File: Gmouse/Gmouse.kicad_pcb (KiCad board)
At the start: 2 copper layers, 80 x 100 mm, 79 parts, among them J1 Motor_RF, J2 Motor_RR, J3 Motor_LF, J4 Motor_LR, J5 Conn_01x08_Pin, Q10 SFH300, Q12 SFH300, Q14 BC847, Q2 SFH300, Q4 SFH300, Q6 SFH300, Q8 SFH300, U1 Teensy4.0, U2 TB6612FNG, U3 L78L05_SOT89, U4 HCMS-2903, U5 TB6612FNG, U7 LD1117S33TR_SOT223

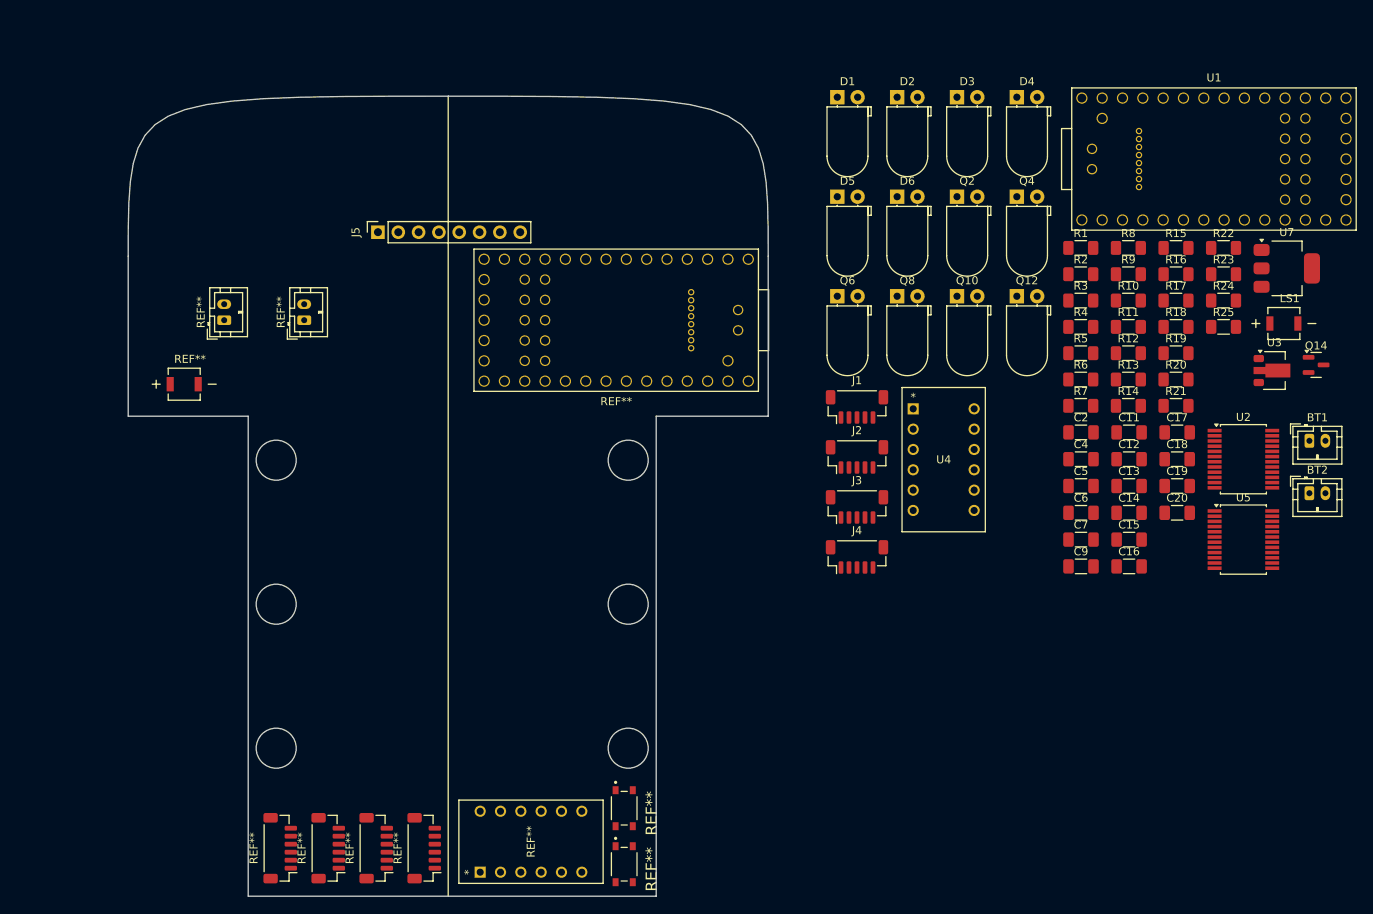
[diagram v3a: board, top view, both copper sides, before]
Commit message: starts pcb design and assigns ton of pins
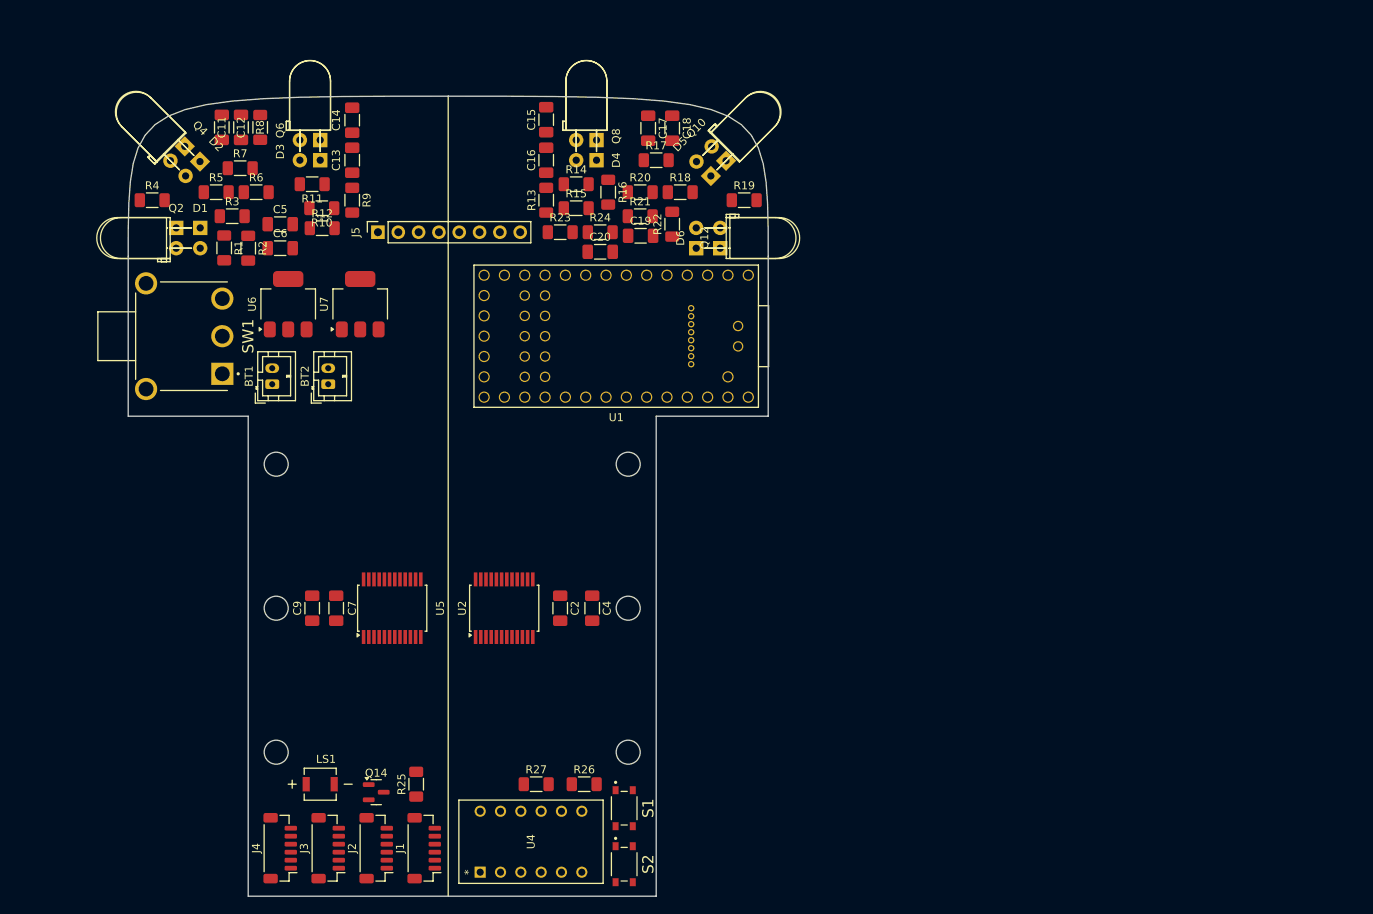
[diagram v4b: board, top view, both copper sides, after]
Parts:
- removed REF** (x2): JST_PH_B2B-PH-K_1x02_P2.00mm_Vertical, Connector_JST:JST_PH_B2B-PH-K_1x02_P2.00mm_Vertical
- removed REF** (x4): JST_SH_BM06B-SRSS-TB_1x06-1MP_P1.00mm_Vertical, Connector_JST:JST_SH_BM06B-SRSS-TB_1x06-1MP_P1.00mm_Vertical
- removed REF**: DIP12_HCMS-290X-A_BRA, HCMS_2903:DIP12_HCMS-290X-A_BRA
- removed REF**: Teensy 4.0, Teensy:Teensy40_SMT
- removed REF** (x2): SW_TL3365AF180QG, Buttons:SW_TL3365AF180QG
- removed REF**: XDCR_SMT-0440-T-R, SMT_0440:XDCR_SMT-0440-T-R
- removed U3: L78L05_SOT89, Package_TO_SOT_SMD:SOT-89-3
- added R26: 10K, Resistor_SMD:R_1206_3216Metric_Pad1.30x1.75mm_HandSolder, F.Cu at (111.0, 126.0)
- added R27: 10K, Resistor_SMD:R_1206_3216Metric_Pad1.30x1.75mm_HandSolder, F.Cu at (105.0, 126.0)
- added S1: TL3365AF180QG, Buttons:SW_TL3365AF180QG, F.Cu at (116.0, 129.0)
- added S2: TL3365AF180QG, Buttons:SW_TL3365AF180QG, F.Cu at (116.0, 136.0)
- added SW1: SW_SPDT, Switch:SW_500SSP1S1M6QEA, F.Cu at (61.0, 70.0)
- added U6: LD1117S50TR_SOT223, Package_TO_SOT_SMD:SOT-223-3_TabPin2, F.Cu at (74.0, 66.0)
- D1, D2, D3, D4, D5, D6: footprint LED_THT:LED_D5.0mm_Horizontal_O1.27mm_Z9.0mm -> LED_THT:LED_D5.0mm_Horizontal_O3.81mm_Z9.0mm
- J1, J2, J3, J4: footprint Connector_JST:JST_SH_BM05B-SRSS-TB_1x05-1MP_P1.00mm_Vertical -> Connector_JST:JST_SH_BM06B-SRSS-TB_1x06-1MP_P1.00mm_Vertical
- moved LS1 133.5 mm to (78.0, 126.0)
- moved BT1 129.8 mm to (72.0, 76.0), turned to 90 degrees
- moved Q14 129.1 mm to (85.0, 127.0)
- moved BT2 123.4 mm to (79.0, 76.0), turned to 90 degrees
- moved C11 119.6 mm to (65.7, 43.9), turned to -90 degrees
- moved C12 118.5 mm to (68.1, 43.9), turned to -90 degrees
- moved R4 117.1 mm to (57.0, 53.0)
- moved R25 116.0 mm to (90.0, 126.0), turned to 90 degrees
- moved U7 115.9 mm to (83.0, 66.0), turned to 90 degrees
- moved R5 109.9 mm to (65.0, 52.0)
- moved R8 109.6 mm to (70.5, 43.9), turned to 90 degrees
- moved R7 109.2 mm to (68.0, 49.0)
- moved C14 108.8 mm to (82.0, 43.0), turned to 90 degrees
- moved R1 107.1 mm to (66.0, 59.0), turned to -90 degrees
- moved U5 106.7 mm to (87.0, 104.0), turned to 90 degrees
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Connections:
- J5 pad 1: unconnected-(J5-Pin_1-Pad1) -> +5V
- J5 pad 3: unconnected-(J5-Pin_3-Pad3) -> GND
- J5 pad 4: unconnected-(J5-Pin_4-Pad4) -> Gyro_SCL
- J5 pad 5: unconnected-(J5-Pin_5-Pad5) -> Gyro_SDA
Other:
- outline, holes or cut-outs redrawn
- copper layers 2 -> 4

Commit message: cleaned up IR Emitter Circuit
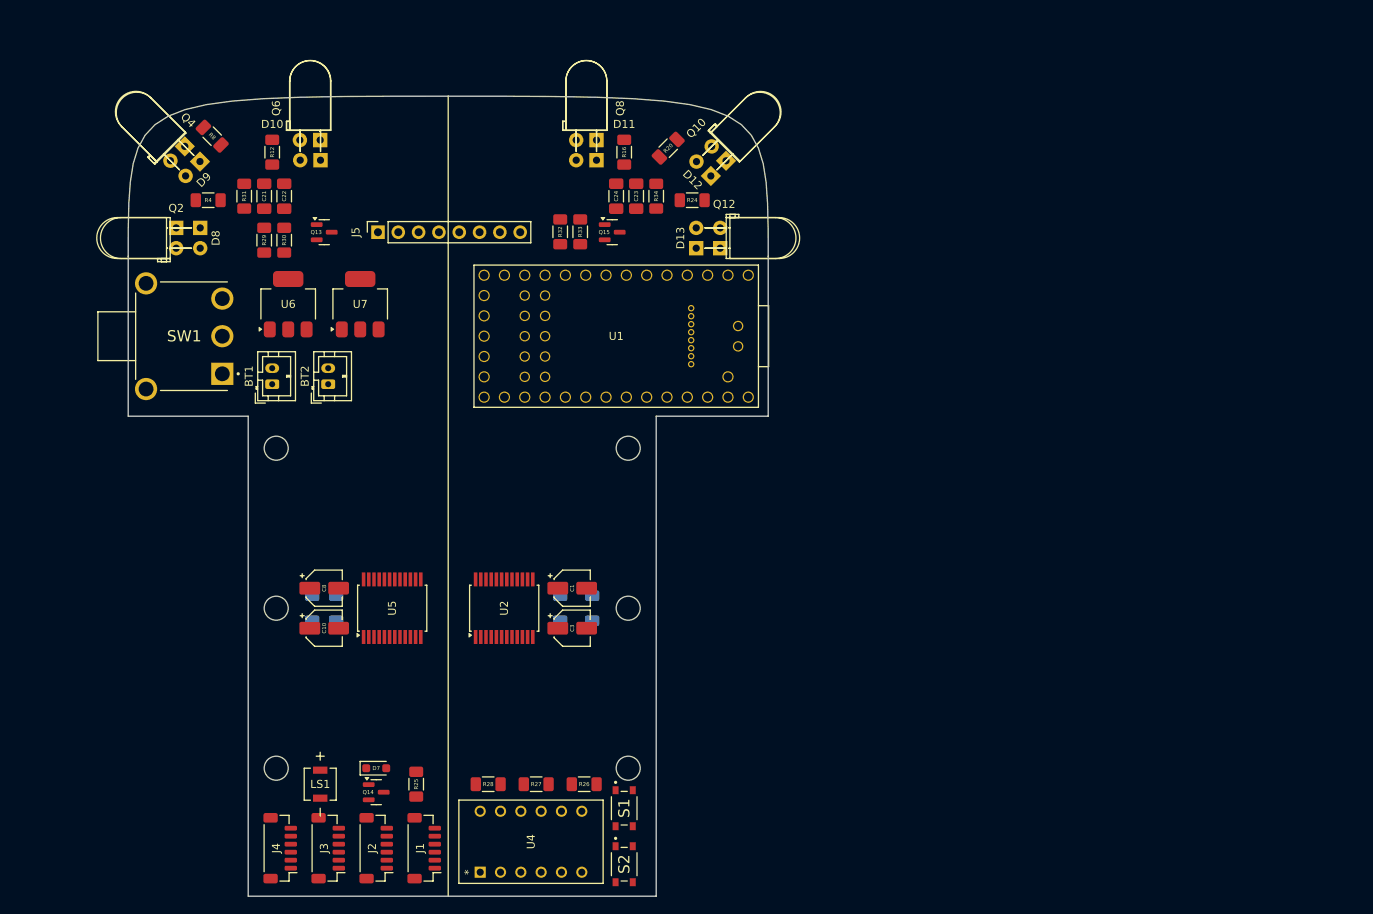
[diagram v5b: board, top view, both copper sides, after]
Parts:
- removed C11, C13, C15, C17, C19, C5: 4.7uF, Capacitor_SMD:C_1206_3216Metric_Pad1.33x1.80mm_HandSolder
- removed C12, C14, C16, C18, C20, C6: 0.1uF, Capacitor_SMD:C_1206_3216Metric_Pad1.33x1.80mm_HandSolder
- removed D1, D2, D3, D4, D5, D6: IR, LED_THT:LED_D5.0mm_Horizontal_O3.81mm_Z9.0mm
- removed R1, R10, R14, R18, R22, R6: 47K, Resistor_SMD:R_1206_3216Metric_Pad1.30x1.75mm_HandSolder
- removed R11, R15, R19, R23, R3, R7: 51, Resistor_SMD:R_1206_3216Metric_Pad1.30x1.75mm_HandSolder
- removed R13, R17, R2, R21, R5, R9: 100, Resistor_SMD:R_1206_3216Metric_Pad1.30x1.75mm_HandSolder
- added C1: 10 uF, Capacitor_SMD:CP_Elec_4x5.4, F.Cu at (109.5, 101.5)
- added C10: 10 uF, Capacitor_SMD:CP_Elec_4x5.4, F.Cu at (78.5, 106.5)
- added C21: 4.7uF, Capacitor_SMD:C_1206_3216Metric_Pad1.33x1.80mm_HandSolder, F.Cu at (71.0, 52.5)
- added C22: 0.1uF, Capacitor_SMD:C_1206_3216Metric_Pad1.33x1.80mm_HandSolder, F.Cu at (73.5, 52.5)
- added C23: 4.7uF, Capacitor_SMD:C_1206_3216Metric_Pad1.33x1.80mm_HandSolder, F.Cu at (117.5, 52.5)
- added C24: 0.1uF, Capacitor_SMD:C_1206_3216Metric_Pad1.33x1.80mm_HandSolder, F.Cu at (115.0, 52.5)
- added C3: 10 uF, Capacitor_SMD:CP_Elec_4x5.4, F.Cu at (109.5, 106.5)
- added C8: 10 uF, Capacitor_SMD:CP_Elec_4x5.4, F.Cu at (78.5, 101.5)
- added D10: IR, LED_THT:LED_D5.0mm_Horizontal_O3.81mm_Z9.0mm, F.Cu at (78.0, 48.0)
- added D11: IR, LED_THT:LED_D5.0mm_Horizontal_O3.81mm_Z9.0mm, F.Cu at (112.5, 48.0)
- added D12: IR, LED_THT:LED_D5.0mm_Horizontal_O3.81mm_Z9.0mm, F.Cu at (126.8, 50.0)
- added D13: IR, LED_THT:LED_D5.0mm_Horizontal_O3.81mm_Z9.0mm, F.Cu at (125.0, 59.0)
- added D7: D, Diode_SMD:D_SOD-323_HandSoldering, F.Cu at (85.0, 124.0)
- added D8: IR, LED_THT:LED_D5.0mm_Horizontal_O3.81mm_Z9.0mm, F.Cu at (63.0, 56.5)
- added D9: IR, LED_THT:LED_D5.0mm_Horizontal_O3.81mm_Z9.0mm, F.Cu at (63.0, 48.2)
- added Q13: NMOS, Package_TO_SOT_SMD:SOT-23, F.Cu at (78.5, 57.0)
- added Q15: NMOS, Package_TO_SOT_SMD:SOT-23, F.Cu at (114.5, 57.0)
- added R28: 10K, Resistor_SMD:R_1206_3216Metric_Pad1.30x1.75mm_HandSolder, F.Cu at (99.0, 126.0)
- added R29: 100, Resistor_SMD:R_1206_3216Metric_Pad1.30x1.75mm_HandSolder, F.Cu at (71.0, 58.0)
- added R30: 47K, Resistor_SMD:R_1206_3216Metric_Pad1.30x1.75mm_HandSolder, F.Cu at (73.5, 58.0)
- added R31: 51, Resistor_SMD:R_1206_3216Metric_Pad1.30x1.75mm_HandSolder, F.Cu at (68.5, 52.5)
- added R32: 100, Resistor_SMD:R_1206_3216Metric_Pad1.30x1.75mm_HandSolder, F.Cu at (108.0, 57.0)
- added R33: 47K, Resistor_SMD:R_1206_3216Metric_Pad1.30x1.75mm_HandSolder, F.Cu at (110.5, 57.0)
- added R34: 51, Resistor_SMD:R_1206_3216Metric_Pad1.30x1.75mm_HandSolder, F.Cu at (120.0, 52.5)
- C2, C4, C7, C9: moved to B.Cu
- moved R24 12.2 mm to (124.5, 53.0), turned to 180 degrees
- moved R12 11.4 mm to (72.0, 47.0), turned to -90 degrees
- moved R4 7.00 mm to (64.0, 53.0)
- moved R20 6.52 mm to (121.5, 46.5), turned to -135 degrees
- moved R8 6.10 mm to (64.5, 45.0), turned to -45 degrees
- moved R16 5.39 mm to (116.0, 47.0)
- turned LS1 to -90 degrees
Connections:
- net Motor1_M1 renamed Motor_RF_M1
- net Motor1_M2 renamed Motor_RF_M2
- net Motor2_M1 renamed Motor_RR_M1
- net Motor2_M2 renamed Motor_RR_M2
- J1 pad 2: Motor1_OutB -> Motor_RF_OutB
- J1 pad 3: Motor1_OutA -> Motor_RF_OutA
- J2 pad 2: Motor2_OutB -> Motor_RR_OutB
- J2 pad 3: Motor2_OutA -> Motor_RR_OutA
- U1 pad 10: unconnected-(U1-8_TX2_IN1-Pad10) -> Motor_STBY
- U1 pad 11: unconnected-(U1-9_OUT1C-Pad11) -> Speaker Signal
- U1 pad 12: unconnected-(U1-10_CS_MQSR-Pad12) -> HCMS_CE
- U1 pad 13: unconnected-(U1-11_MOSI_CTX1-Pad13) -> HCMS_DataIn
- U1 pad 14: unconnected-(U1-12_MISO_MQSL-Pad14) -> HCMS_RS
- U1 pad 20: unconnected-(U1-13_SCK_CRX1_LED-Pad20) -> HCMS_CLK
- U1 pad 21: unconnected-(U1-14_A0_TX3_SPDIF_OUT-Pad21) -> Motor_RF_OutA
- U1 pad 22: unconnected-(U1-15_A1_RX3_SPDIF_IN-Pad22) -> Motor_RF_OutB
- U1 pad 23: unconnected-(U1-16_A2_RX4_SCL1-Pad23) -> Gyro_SCL
- U1 pad 24: unconnected-(U1-17_A3_TX4_SDA1-Pad24) -> Gyro_SDA
- U1 pad 25: unconnected-(U1-18_A4_SDA0-Pad25) -> IR_Reciever_Left_90
- U1 pad 26: unconnected-(U1-19_A5_SCL0-Pad26) -> IR_Reciever_Left_45
- U1 pad 27: unconnected-(U1-20_A6_TX5_LRCLK1-Pad27) -> IR_Reciever_Left_0
- U1 pad 28: unconnected-(U1-21_A7_RX5_BCLK1-Pad28) -> IR_Reciever_Right_0
- U1 pad 29: unconnected-(U1-22_A8_CTX1-Pad29) -> IR_Reciever_Right_45
- U1 pad 30: unconnected-(U1-23_A9_CRX1_MCLK1-Pad30) -> IR_Reciever_Right_90
- U1 pad 35: unconnected-(U1-24_A10_TX6_SCL2-Pad35) -> Left_IN1
- U1 pad 36: unconnected-(U1-25_A11_RX6_SDA2-Pad36) -> Right_IN1
- U1 pad 37: unconnected-(U1-26_A12_MOSI1-Pad37) -> Left_IN2
- U1 pad 38: unconnected-(U1-27_A13_SCK1-Pad38) -> Right_IN2
- U1 pad 39: unconnected-(U1-28_RX7-Pad39) -> Motor_RR_OutA
- U1 pad 40: unconnected-(U1-29_TX7-Pad40) -> Motor_RR_OutB
- U1 pad 41: unconnected-(U1-30_CRX3-Pad41) -> Motor_LF_OutA
- U1 pad 42: unconnected-(U1-31_CTX3-Pad42) -> Motor_LF_OutB
- U1 pad 43: unconnected-(U1-32_OUT1B-Pad43) -> Motor_LR_OutA
- U1 pad 44: unconnected-(U1-33_MCLK2-Pad44) -> Motor_LR_OutB
- U1 pad 45: unconnected-(U1-34_DAT1_MISO2-Pad45) -> Interface_Button1
- U1 pad 46: unconnected-(U1-35_DAT0_MOSI2-Pad46) -> Interface_Button2
- U1 pad 6: unconnected-(U1-4_BCLK2-Pad6) -> Motor_RF_PWM
- U1 pad 7: unconnected-(U1-5_IN2-Pad7) -> Motor_RR_PWM
- U1 pad 8: unconnected-(U1-6_OUT1D-Pad8) -> Motor_LF_PWM
- U1 pad 9: unconnected-(U1-7_RX2_OUT1A-Pad9) -> Motor_LR_PWM
- U2 pad 15: Motor2_PWM -> Motor_RR_PWM
- U2 pad 23: Motor1_PWM -> Motor_RF_PWM
- U4 pad 10: +5V -> +3V3
- U4 pad 11: +5V -> +3V3
- U4 pad 12: HCMS_Reset -> Net-(U4-*RESET)
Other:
- outline, holes or cut-outs redrawn

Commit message: Started adding traces
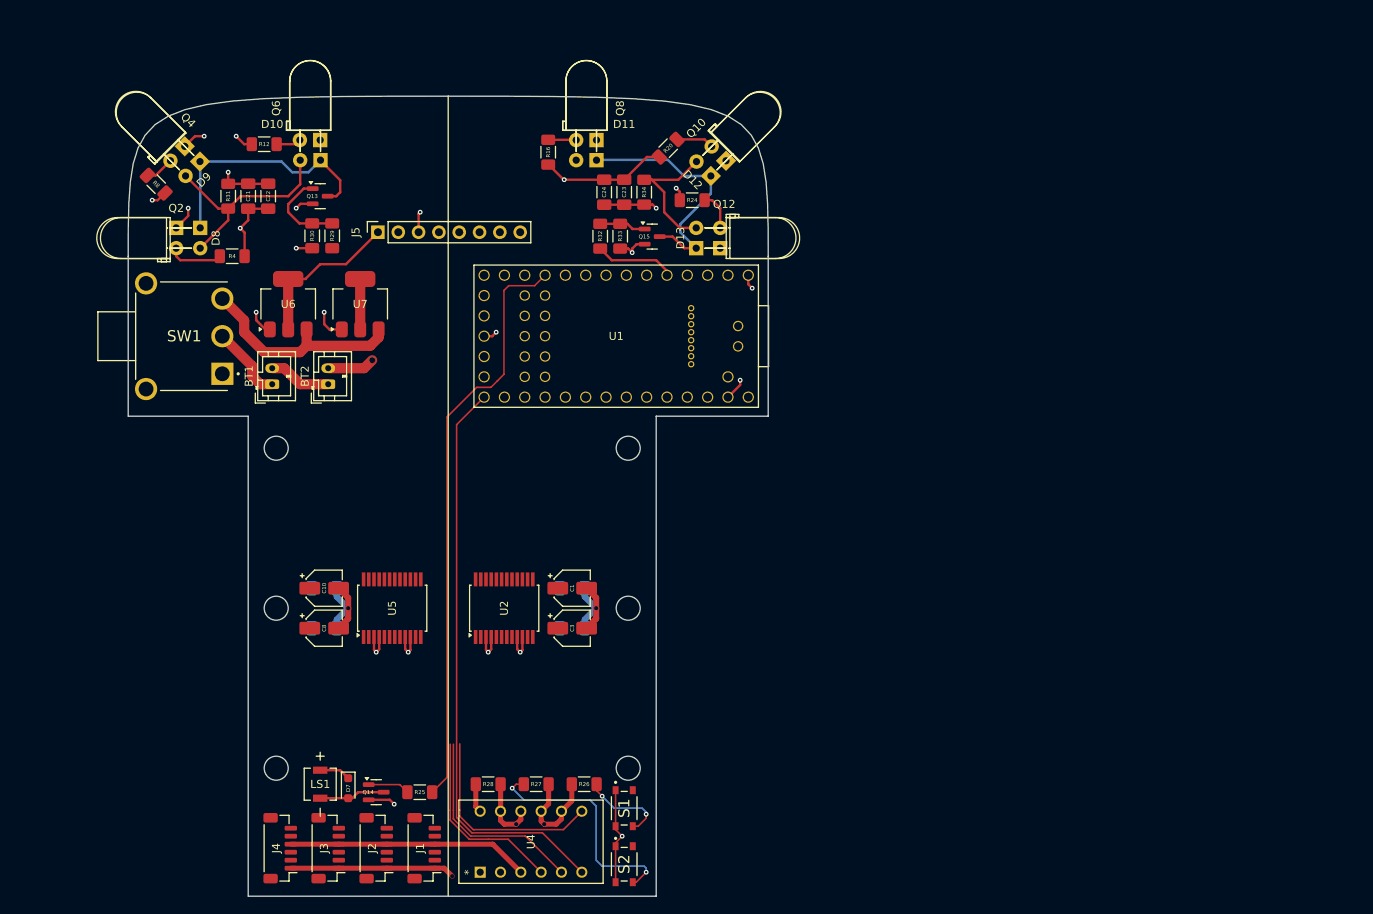
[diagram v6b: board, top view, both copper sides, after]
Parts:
- moved R16 9.50 mm to (106.5, 47.0)
- moved R8 9.22 mm to (57.5, 51.0)
- moved R29 8.52 mm to (79.5, 57.5)
- moved R4 7.62 mm to (67.0, 60.0)
- moved Q15 5.03 mm to (119.5, 57.5)
- moved R32 5.03 mm to (113.0, 57.5)
- moved R33 5.03 mm to (115.5, 57.5)
- moved C10 5.00 mm to (78.5, 101.5)
- moved C8 5.00 mm to (78.5, 106.5)
- moved Q13 4.53 mm to (78.0, 52.5)
- moved D7 4.30 mm to (81.5, 126.5), turned to -90 degrees
- moved R30 3.54 mm to (77.0, 57.5)
- moved C4 3.54 mm to (109.5, 106.5), turned to 0 degrees
- moved C2 2.92 mm to (109.5, 101.5), turned to 0 degrees
- moved C7 2.92 mm to (78.5, 106.5), turned to 0 degrees
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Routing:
- net GND: track 0.00 -> 138.7 mm, vias 0 -> 24
- net Speaker Signal: track 0.00 -> 73.4 mm
- net HCMS_CLK: track 0.00 -> 72.4 mm
- net +5V: track 0.00 -> 50.1 mm
- net +3V3: track 0.00 -> 50.1 mm, vias 0 -> 6
- net Net-(D11-K): track 0.00 -> 31.8 mm
- net Net-(D10-K): track 0.00 -> 31.3 mm
- net Net-(R27-Pad1): track 0.00 -> 29.2 mm, vias 0 -> 2
- net +BATT: track 0.00 -> 27.0 mm
- net Net-(D10-A): track 0.00 -> 26.7 mm
- net HCMS_CE: track 0.00 -> 25.9 mm
- net HCMS_RS: track 0.00 -> 25.6 mm
- net HCMS_DataIn: track 0.00 -> 23.6 mm
- net Net-(D11-A): track 0.00 -> 17.9 mm
- net Net-(R26-Pad2): track 0.00 -> 11.0 mm, vias 0 -> 2
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
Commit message: Lot of Manual Routing
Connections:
- C3 pad 1: +5V -> +3V3
- C4 pad 1: +5V -> +3V3
- C7 pad 1: +5V -> +3V3
- C8 pad 1: +5V -> +3V3
- J1 pad 4: +5V -> +3V3
- J2 pad 4: +5V -> +3V3
- J3 pad 4: +5V -> +3V3
- J4 pad 4: +5V -> +3V3
- J5 pad 1: +5V -> +3V3
- U1 pad 39: Motor_RR_OutA -> Motor_RR_OutB
- U1 pad 40: Motor_RR_OutB -> Motor_RR_OutA
- U1 pad 41: Motor_LF_OutA -> Motor_LF_OutB
- U1 pad 42: Motor_LF_OutB -> Motor_LF_OutA
- U1 pad 43: Motor_LR_OutA -> Motor_LR_OutB
- U1 pad 44: Motor_LR_OutB -> Motor_LR_OutA
- U2 pad 20: +5V -> +3V3
- U5 pad 20: +5V -> +3V3
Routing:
- net +5V: track 50.1 -> 197.7 mm, vias 0 -> 1
- net +BATT: track 27.0 -> 152.9 mm, vias 0 -> 4
- net Motor_LR_OutB: track 0.00 -> 104.1 mm, vias 0 -> 1
- net Motor_LR_OutA: track 0.00 -> 102.6 mm, vias 0 -> 1
- net Motor_LF_OutA: track 0.00 -> 94.3 mm, vias 0 -> 3
- net Motor_LF_OutB: track 0.00 -> 93.9 mm, vias 0 -> 4
- net IR_Reciever_Left_45: track 3.63 -> 89.4 mm, vias 0 -> 2
- net Motor_STBY: track 0.00 -> 74.9 mm, vias 0 -> 3
- net IR_Reciever_Left_0: track 3.12 -> 75.9 mm, vias 0 -> 1
- net Interface_Button2: track 0.00 -> 72.8 mm
- net IR_Reciever_Left_90: track 6.86 -> 71.5 mm, vias 0 -> 1
- net HCMS_CE: track 25.9 -> 90.4 mm, vias 0 -> 2
- net HCMS_DataIn: track 23.6 -> 86.3 mm
- net HCMS_RS: track 25.6 -> 85.8 mm, vias 0 -> 2
- net Interface_Button1: track 0.00 -> 60.0 mm
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- added copper zone on In1.Cu, net +3V3
- added copper zone on In2.Cu, net GND

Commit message: V1 Finished
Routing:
- net Motor_RR_OutA: track 0.00 -> 79.3 mm, vias 0 -> 1
- net Motor_RR_OutB: track 0.00 -> 74.4 mm, vias 0 -> 1
- net Motor_RF_OutB: track 0.00 -> 63.5 mm, vias 0 -> 1
- net Motor_RF_OutA: track 0.00 -> 60.9 mm, vias 0 -> 1
- net Motor_LR_PWM: track 26.9 -> 84.6 mm, vias 0 -> 2
- net Left_IN2: track 0.00 -> 49.9 mm, vias 0 -> 2
- net Motor_LF_PWM: track 24.7 -> 69.2 mm, vias 0 -> 3
- net Left_IN1: track 0.00 -> 40.0 mm, vias 0 -> 3
- net Right_IN2: track 18.8 -> 45.3 mm
- net Right_IN1: track 11.8 -> 37.2 mm
- net GND: track 126.0 -> 132.0 mm, vias 28 -> 32
- net IR_Reciever_Right_45: track 41.5 -> 43.7 mm
- net Net-(D11-A): track 29.7 -> 31.3 mm
- net IR_Reciever_Left_45: track 89.4 -> 90.5 mm
- net Net-(D11-K): track 31.8 -> 32.9 mm
